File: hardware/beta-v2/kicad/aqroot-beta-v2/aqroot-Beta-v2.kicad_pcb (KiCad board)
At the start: 6 copper layers, 72 x 148 mm, 324 parts, among them J1 FH69-50S-0.5SH, J2 Molex_5025700893, J3 USB_C_Receptacle_USB2.0_16P, J4 JST-PH-2 BATTERY, J5 COMMUNITY_PORT_1x24, J6 JST-PH-2 SPEAKER, J7 BM02B-ACHSS-GAN-ETF, J8 QWIIC_STEMMA_QT, Q1 AO3400A, Q10 2N7002, Q2 NTMD4820N, Q3 NTMD4820N, Q4 BSS138, Q5 AO3401A, Q6 BSS138, Q7 BSS138, Q8 BSS138, Q9 BSS138, SW1 BOOT, SW2 UP, SW3 DOWN, SW4 LEFT, SW5 RIGHT, SW6 A_SELECT, SW7 B_BACK, SW9 SW_SPDT, U1 ESP32-S3-WROOM-1, U10 USBLC6-2SC6, U11 BQ25185, U12 TPS63020, U13 TPS61023, U14 MAX17048, U16 TCA4307DGKR, U17 TPS61169DCKR, U18 LTC4368-1, U19 TLV7032, U2 PCAL9535APW, U20 TPS22950C, U21 TPS61023, U22 TPS22950C, U23 PCAL9535APW, U3 PCAL9535APW, U4 BMI270, U5 MAX98357A, U6 TSOP38238, U7 E07-400M10S, U8 E22-900M22S, U9 ST25R3916-AQET, Y1 27.12MHz 10pF 3225-4P

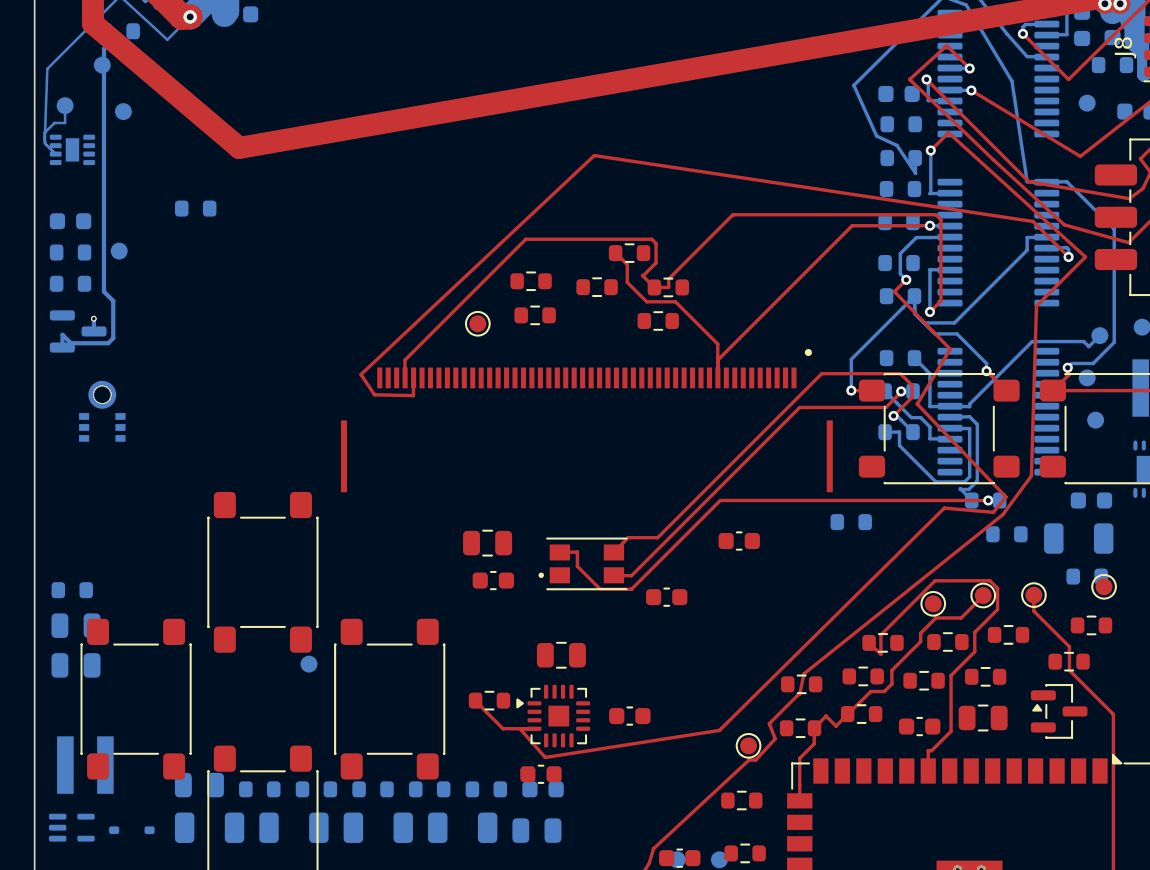
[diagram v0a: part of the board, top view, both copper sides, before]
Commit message: FBV2-P2-030: promote BTN_RIGHT_N hop-anchor route
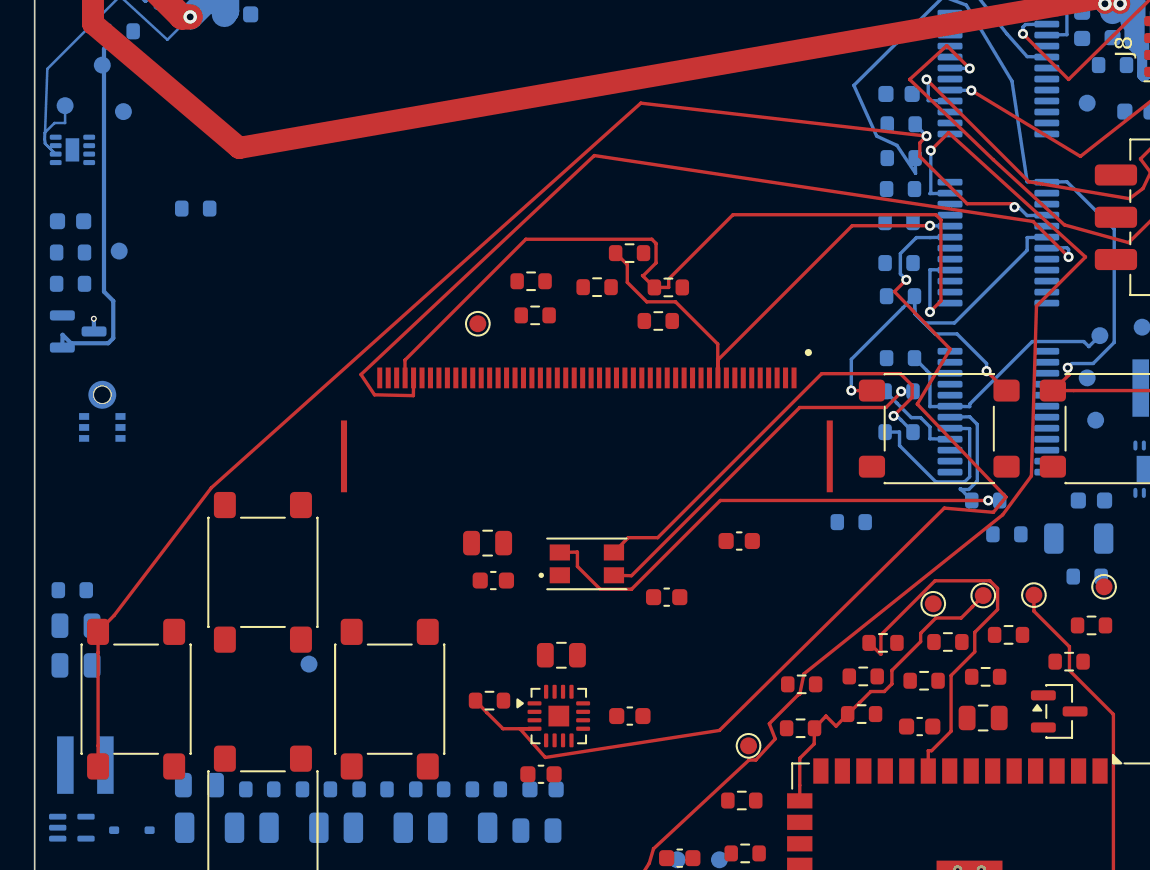
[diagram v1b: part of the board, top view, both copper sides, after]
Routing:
- net /08_BUTTONS_EXPANDERS/BTN_RIGHT_N: track 0.00 -> 81.2 mm, vias 0 -> 2
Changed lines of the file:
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@@
+	)
+	(segment
+		(start 3.75 111.02)
+		(end 3.75 112.25)
+		(width 0.2)
+		(layer "F.Cu")
+		(net "/08_BUTTONS_EXPANDERS/BTN_RIGHT_N")
+	)
+	(segment
+		(start 52.35 82.1)
+		(end 52.35 82.9)
+		(width 0.2)
+		(layer "F.Cu")
+		(net "/08_BUTTONS_EXPANDERS/BTN_RIGHT_N")
+	)
+	(segment
+		(start 3.75 112.25)
+		(end 3.75 117.75)
+		(width 0.2)
+		(layer "F.Cu")
+		(net "/08_BUTTONS_EXPANDERS/BTN_RIGHT_N")
+	)
+	(segment
+		(start 10.45 102.5)
+		(end 35.85 79.75)
+		(width 0.2)
+		(layer "F.Cu")
+		(net "/08_BUTTONS_EXPANDERS/BTN_RIGHT_N")
+	)
+	(segment
+		(start 55.15 85.7)
+		(end 57.75 85.7)
+		(width 0.2)
+		(layer "F.Cu")
+		(net "/08_BUTTONS_EXPANDERS/BTN_RIGHT_N")
+	)
+	(segment
+		(start 4.7 110.05)
+		(end 10.45 102.5)
+		(width 0.2)
+		(layer "F.Cu")
+		(net "/08_BUTTONS_EXPANDERS/BTN_RIGHT_N")
+	)
+	(segment
+		(start 3.75 118.98)
+		(end 3.75 117.75)
+		(width 0.2)
+		(layer "F.Cu")
+		(net "/08_BUTTONS_EXPANDERS/BTN_RIGHT_N")
+	)
+	(segment
+		(start 52.75 81.7)
+		(end 52.35 82.1)
+		(width 0.2)
+		(layer "F.Cu")
+		(net "/08_BUTTONS_EXPANDERS/BTN_RIGHT_N")
+	)
+	(segment
+		(start 3.75 111.02)
+		(end 4.7 110.05)
+		(width 0.2)
+		(layer "F.Cu")
+		(net "/08_BUTTONS_EXPANDERS/BTN_RIGHT_N")
+	)
+	(segment
+		(start 52.35 82.9)
+		(end 55.15 85.7)
+		(width 0.2)
+		(layer "F.Cu")
+		(net "/08_BUTTONS_EXPANDERS/BTN_RIGHT_N")
+	)
+	(segment
+		(start 57.75 85.7)
+		(end 57.95 85.9)
+		(width 0.2)
+		(layer "F.Cu")
+		(net "/08_BUTTONS_EXPANDERS/BTN_RIGHT_N")
+	)
+	(segment
+		(start 35.85 79.75)
+		(end 52.75 81.7)
+		(width 0.2)
+		(layer "F.Cu")
+		(net "/08_BUTTONS_EXPANDERS/BTN_RIGHT_N")
+	)
+	(via
+		(at 57.95 85.9)
+		(size 0.6)
+		(drill 0.3)
+		(layers "F.Cu" "B.Cu")
+		(net "/08_BUTTONS_EXPANDERS/BTN_RIGHT_N")
+	)
+	(via
+		(at 52.75 81.7)
+		(size 0.6)
+		(drill 0.3)
+		(layers "F.Cu" "B.Cu")
+		(net "/08_BUTTONS_EXPANDERS/BTN_RIGHT_N")
+	)
+	(segment
+		(start 52.075 81)
+		(end 52.75 81.7)
+		(width 0.2)
+		(layer "B.Cu")
+		(net "/08_BUTTONS_EXPANDERS/BTN_RIGHT_N")
+	)
+	(segment
+		(start 59.8625 86.375)
+		(end 58.7 86.4)
+		(width 0.2)
+		(layer "B.Cu")
+		(net "/08_BUTTONS_EXPANDERS/BTN_RIGHT_N")
+	)
+	(segment
+		(start 58.2 85.9)
+		(end 57.95 85.9)
+		(width 0.2)
+		(layer "B.Cu")
+		(net "/08_BUTTONS_EXPANDERS/BTN_RIGHT_N")
+	)
+	(segment
+		(start 58.7 86.4)
+		(end 58.2 85.9)
+		(width 0.2)
+		(layer "B.Cu")
+		(net "/08_BUTTONS_EXPANDERS/BTN_RIGHT_N")
 	)
 	(segment

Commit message: FBV2-P2-033: promote In2 XGPIO2 framework pilot (D-331)
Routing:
- net /XGPIO2: track 0.00 -> 53.8 mm, vias 0 -> 2
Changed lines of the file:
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@@
+	)
+	(segment
+		(start 54.962913 26.395745)
+		(end 54.95 27.3)
+		(width 0.2)
+		(layer "F.Cu")
+		(net "/XGPIO2")
+	)
+	(segment
+		(start 54.95 27.3)
+		(end 55 27.3)
+		(width 0.2)
+		(layer "F.Cu")
+		(net "/XGPIO2")
+	)
+	(via
+		(at 55.9 78.3)
+		(size 0.6)
+		(drill 0.3)
+		(layers "F.Cu" "B.Cu")
+		(net "/XGPIO2")
+	)
+	(via
+		(at 55 27.3)
+		(size 0.6)
+		(drill 0.3)
+		(layers "F.Cu" "B.Cu")
+		(net "/XGPIO2")
+	)
+	(segment
+		(start 55.3 78.35)
+		(end 55.85 78.35)
+		(width 0.2)
+		(layer "B.Cu")
+		(net "/XGPIO2")
+	)
+	(segment
+		(start 55.85 78.35)
+		(end 55.9 78.3)
+		(width 0.2)
+		(layer "B.Cu")
+		(net "/XGPIO2")
+	)
+	(segment
+		(start 54.1375 78.325)
+		(end 55.3 78.3)
+		(width 0.2)
+		(layer "B.Cu")
+		(net "/XGPIO2")
+	)
+	(segment
+		(start 55.3 78.3)
+		(end 55.3 78.35)
+		(width 0.2)
+		(layer "B.Cu")
+		(net "/XGPIO2")
+	)
+	(segment
+		(start 55.95 78.25)
+		(end 55.9 78.3)
+		(width 0.2)
+		(layer "In2.Cu")
+		(net "/XGPIO2")
+	)
+	(segment
+		(start 55 27.3)
+		(end 55.95 78.25)
+		(width 0.2)
+		(layer "In2.Cu")
+		(net "/XGPIO2")
 	)
 	(segment

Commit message: FBV2-P2-034: promote XGPIO4/XGPIO5 inner-haul batch (D-332)
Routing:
- net /XGPIO4: track 0.00 -> 63.0 mm, vias 0 -> 2
- net /XGPIO5: track 0.00 -> 47.6 mm, vias 0 -> 2
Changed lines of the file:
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@@
+	)
+	(segment
+		(start 54.409814 30.836116)
+		(end 53.55 30.85)
+		(width 0.2)
+		(layer "F.Cu")
+		(net "/XGPIO5")
+	)
+	(via
+		(at 53.55 30.85)
+		(size 0.6)
+		(drill 0.3)
+		(layers "F.Cu" "B.Cu")
+		(net "/XGPIO5")
+	)
+	(via
+		(at 55.25 76.35)
+		(size 0.6)
+		(drill 0.3)
+		(layers "F.Cu" "B.Cu")
+		(net "/XGPIO5")
+	)
+	(segment
+		(start 54.1375 76.375)
+		(end 55.3 76.4)
+		(width 0.2)
+		(layer "B.Cu")
+		(net "/XGPIO5")
+	)
+	(segment
+		(start 55.3 76.4)
+		(end 55.25 76.35)
+		(width 0.2)
+		(layer "B.Cu")
+		(net "/XGPIO5")
+	)
+	(segment
+		(start 53.55 30.85)
+		(end 55.25 76.35)
+		(width 0.2)
+		(layer "In2.Cu")
+		(net "/XGPIO5")
 	)
 	(segment
@@
 	)
 	(segment
+		(start 55.149309 21.51856)
+		(end 55.15 22.45)
+		(width 0.2)
+		(layer "F.Cu")
+		(net "/XGPIO4")
+	)
+	(via
+		(at 56.6 77.7)
+		(size 0.6)
+		(drill 0.3)
+		(layers "F.Cu" "B.Cu")
+		(net "/XGPIO4")
+	)
+	(via
+		(at 55.15 22.45)
+		(size 0.6)
+		(drill 0.3)
+		(layers "F.Cu" "B.Cu")
+		(net "/XGPIO4")
+	)
+	(segment
+		(start 55.3 77)
+		(end 55.9 77)
+		(width 0.2)
+		(layer "B.Cu")
+		(net "/XGPIO4")
+	)
+	(segment
+		(start 54.1375 77.025)
+		(end 55.3 77)
+		(width 0.2)
+		(layer "B.Cu")
+		(net "/XGPIO4")
+	)
+	(segment
+		(start 55.9 77)
+		(end 56.6 77.7)
+		(width 0.2)
+		(layer "B.Cu")
+		(net "/XGPIO4")
+	)
+	(segment
+		(start 64.6 67.65)
+		(end 56.4 76.95)
+		(width 0.2)
+		(layer "In2.Cu")
+		(net "/XGPIO4")
+	)
+	(segment
+		(start 56.4 76.95)
+		(end 56.6 77.7)
+		(width 0.2)
+		(layer "In2.Cu")
+		(net "/XGPIO4")
+	)
+	(segment
+		(start 55.15 22.45)
+		(end 64.6 67.65)
+		(width 0.2)
+		(layer "In2.Cu")
+		(net "/XGPIO4")
+	)
+	(segment

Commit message: FBV2-P2-040: promote J1 display fanout (D-338)
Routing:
- net /DISP_CS_N: track 0.00 -> 35.8 mm, vias 0 -> 2
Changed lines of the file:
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@@
+	)
+	(segment
+		(start 26.41 96)
+		(end 26.4 97.05)
+		(width 0.2)
+		(layer "F.Cu")
+		(net "/DISP_CS_N")
+	)
+	(segment
+		(start 42.845742 124.123086)
+		(end 42.85 123.2)
+		(width 0.2)
+		(layer "F.Cu")
+		(net "/DISP_CS_N")
+	)
+	(segment
+		(start 42.845742 124.123086)
+		(end 43.7 124.1)
+		(width 0.2)
+		(layer "F.Cu")
+		(net "/DISP_CS_N")
+	)
+	(segment
+		(start 43.7 124.1)
+		(end 44.05 124.45)
+		(width 0.2)
+		(layer "F.Cu")
+		(net "/DISP_CS_N")
+	)
+	(segment
+		(start 44.05 124.45)
+		(end 44.05 124.8)
+		(width 0.2)
+		(layer "F.Cu")
+		(net "/DISP_CS_N")
+	)
+	(segment
+		(start 45.25 124.825)
+		(end 44.05 124.8)
+		(width 0.2)
+		(layer "F.Cu")
+		(net "/DISP_CS_N")
+	)
+	(via
+		(at 42.85 123.2)
+		(size 0.6)
+		(drill 0.3)
+		(layers "F.Cu" "B.Cu")
+		(net "/DISP_CS_N")
+	)
+	(via
+		(at 26.4 97.05)
+		(size 0.6)
+		(drill 0.3)
+		(layers "F.Cu" "B.Cu")
+		(net "/DISP_CS_N")
+	)
+	(segment
+		(start 42.85 123.2)
+		(end 26.4 97.05)
+		(width 0.2)
+		(layer "In2.Cu")
+		(net "/DISP_CS_N")
 	)
 	(segment

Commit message: FBV2-P2-041: reuse J1 fanout for DISP_DC (D-339)
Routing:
- net /DISP_DC: track 0.00 -> 43.7 mm, vias 0 -> 2
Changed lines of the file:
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@@
+	)
+	(segment
+		(start 45.25 129.905)
+		(end 44.05 129.9)
+		(width 0.2)
+		(layer "F.Cu")
+		(net "/DISP_DC")
+	)
+	(segment
+		(start 26.91 96)
+		(end 26.9 94.95)
+		(width 0.2)
+		(layer "F.Cu")
+		(net "/DISP_DC")
+	)
+	(via
+		(at 44.05 129.9)
+		(size 0.6)
+		(drill 0.3)
+		(layers "F.Cu" "B.Cu")
+		(net "/DISP_DC")
+	)
+	(via
+		(at 26.9 94.95)
+		(size 0.6)
+		(drill 0.3)
+		(layers "F.Cu" "B.Cu")
+		(net "/DISP_DC")
+	)
+	(segment
+		(start 42.4 110.45)
+		(end 26.9 94.95)
+		(width 0.2)
+		(layer "In2.Cu")
+		(net "/DISP_DC")
+	)
+	(segment
+		(start 44.05 129.9)
+		(end 42.4 110.45)
+		(width 0.2)
+		(layer "In2.Cu")
+		(net "/DISP_DC")
 	)
 	(segment

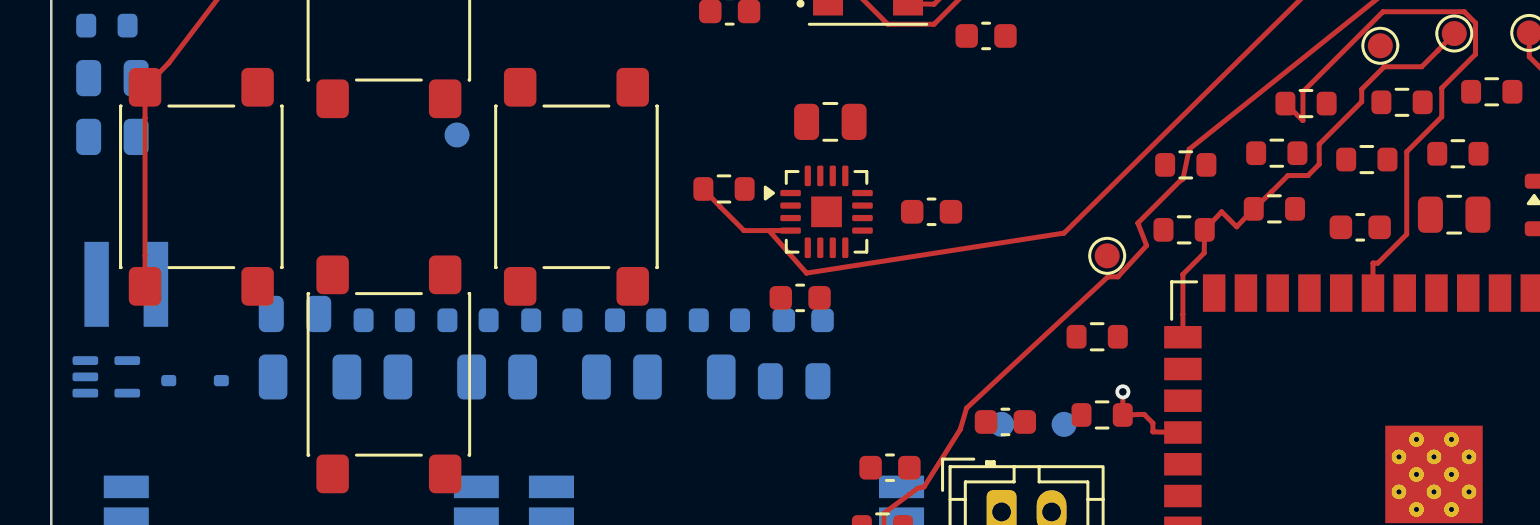
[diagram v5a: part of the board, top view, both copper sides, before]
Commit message: FBV2-P2-045: route boxed backlight control (D-343)
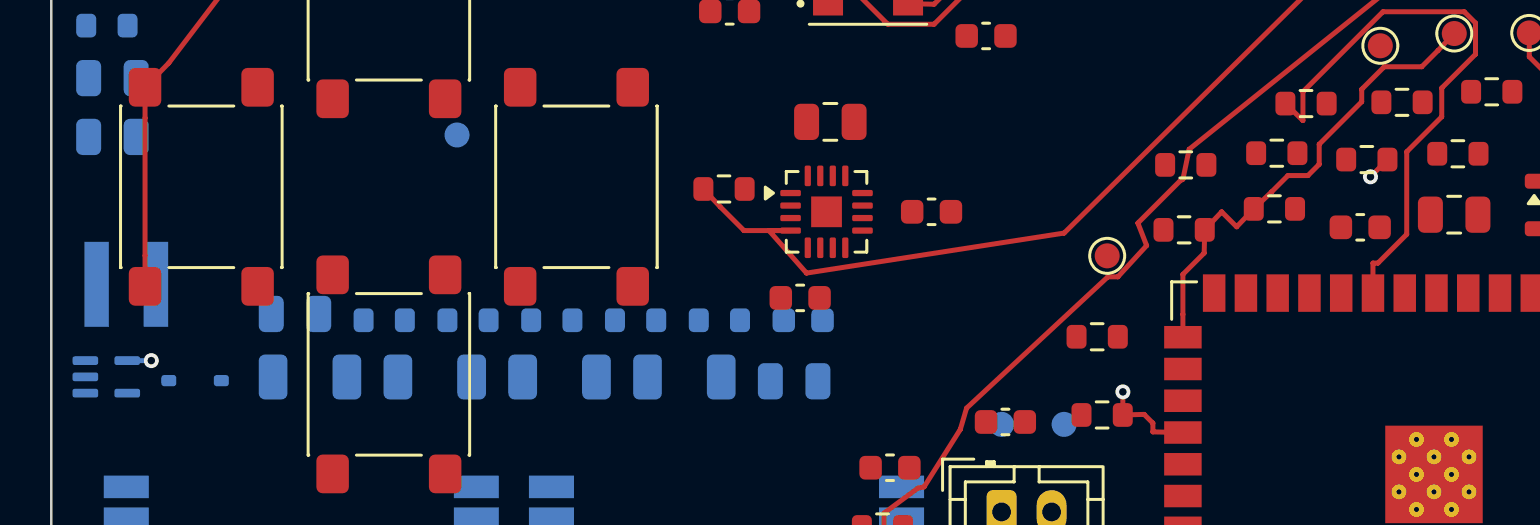
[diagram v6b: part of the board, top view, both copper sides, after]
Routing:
- net /DISP_BL_CTL: track 0.00 -> 51.2 mm, vias 0 -> 2
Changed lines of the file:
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@@
+	)
+	(segment
+		(start 53.429031 113.910322)
+		(end 52.75 114.6)
+		(width 0.2)
+		(layer "F.Cu")
+		(net "/DISP_BL_CTL")
+	)
+	(via
+		(at 4 121.95)
+		(size 0.6)
+		(drill 0.3)
+		(layers "F.Cu" "B.Cu")
+		(net "/DISP_BL_CTL")
+	)
+	(via
+		(at 52.75 114.6)
+		(size 0.6)
+		(drill 0.3)
+		(layers "F.Cu" "B.Cu")
+		(net "/DISP_BL_CTL")
+	)
+	(segment
+		(start 3.0375 121.95)
+		(end 4 121.95)
+		(width 0.2)
+		(layer "B.Cu")
+		(net "/DISP_BL_CTL")
+	)
+	(segment
+		(start 52.75 114.6)
+		(end 4 121.95)
+		(width 0.2)
+		(layer "In3.Cu")
+		(net "/DISP_BL_CTL")
 	)
 	(segment

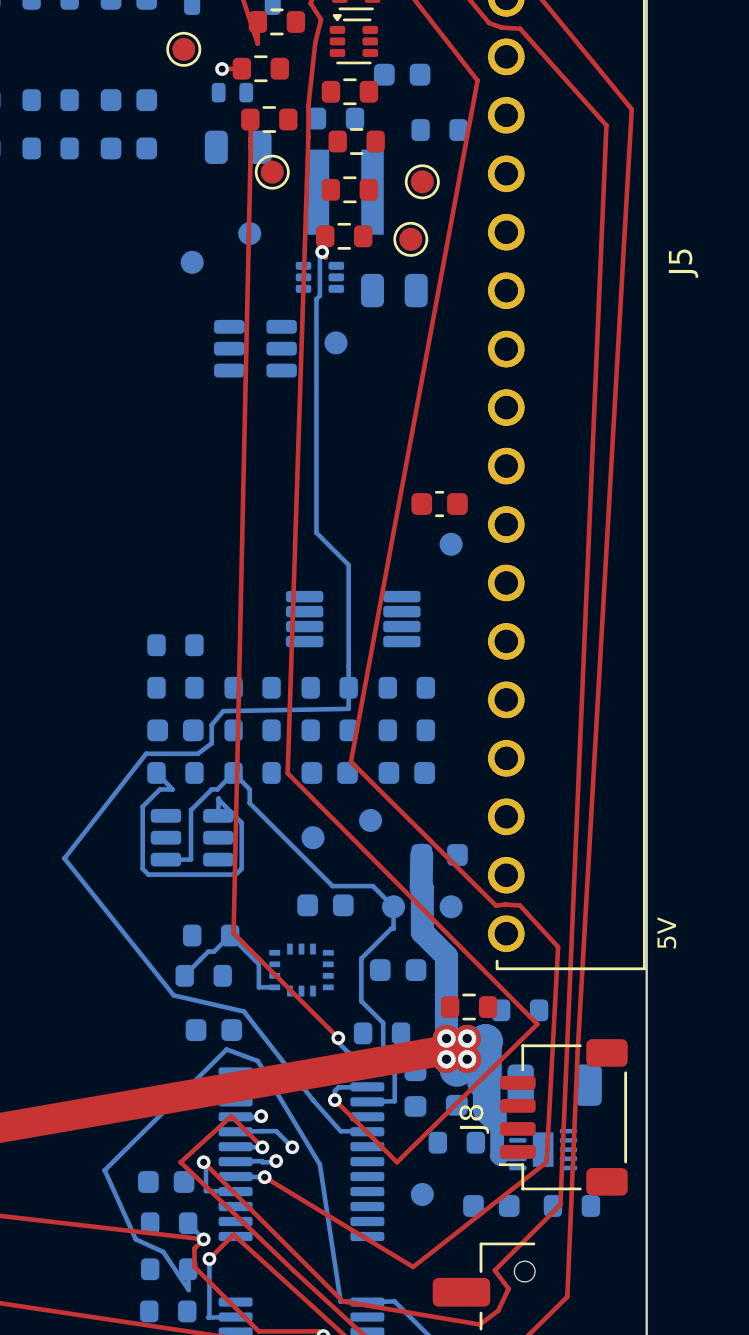
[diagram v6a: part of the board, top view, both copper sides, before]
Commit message: FBV2-P2-055: promote U20 replacement transaction (D-353)
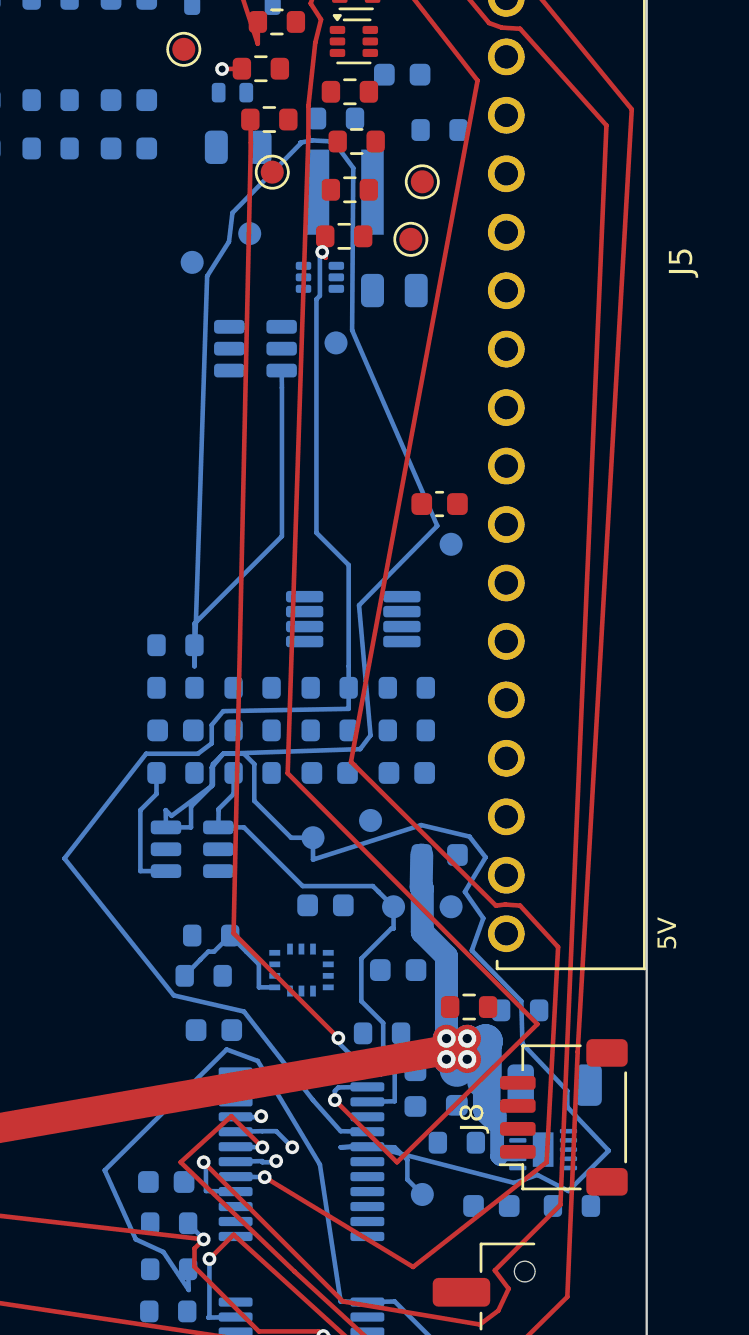
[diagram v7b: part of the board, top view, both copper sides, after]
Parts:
- moved U20 0.50 mm to (52.2, 64.8), turned to 180 degrees
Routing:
- net /ACC_POWER_FAULT_N: track 0.00 -> 133.8 mm
- net /01_POWER_TREE/ACC_3V3_ILIM: track 14.0 -> 5.67 mm
- net /ACC_3V3_EN: track 26.4 -> 22.6 mm
